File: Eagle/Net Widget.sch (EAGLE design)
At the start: 19 parts

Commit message: Switch to Net Widget.lbr and increase hole sizes.
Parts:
- U$2: device Weather Widget:ADAFRUIT-CC3000-BREAKOUT -> Net Widget:ADAFRUIT-CC3000-BREAKOUT
- U$3: device Weather Widget:ADAFRUIT-TFT1.8-BREAKOUT -> Net Widget:ADAFRUIT-TFT1.8-BREAKOUT
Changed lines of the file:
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@@
 <?xml version="1.0" encoding="utf-8"?>
 <!DOCTYPE eagle SYSTEM "eagle.dtd">
-<eagle version="7.1.0">
+<eagle version="7.2.0">
 <drawing>
 <settings>
@@
 <parts>
 <part name="U$1" library="adafruit" deviceset="ATMEGA32U4" device="-AU"/>
-<part name="U$2" library="Weather Widget" deviceset="ADAFRUIT-CC3000-BREAKOUT" device=""/>
-<part name="U$3" library="Weather Widget" deviceset="ADAFRUIT-TFT1.8-BREAKOUT" device=""/>
+<part name="U$2" library="Net Widget" deviceset="ADAFRUIT-CC3000-BREAKOUT" device=""/>
+<part name="U$3" library="Net Widget" deviceset="ADAFRUIT-TFT1.8-BREAKOUT" device=""/>
 <part name="ISP" library="adafruit" deviceset="AVRISP" device="-6"/>
 <part name="CN1" library="adafruit" deviceset="USB" device="MINIB"/>

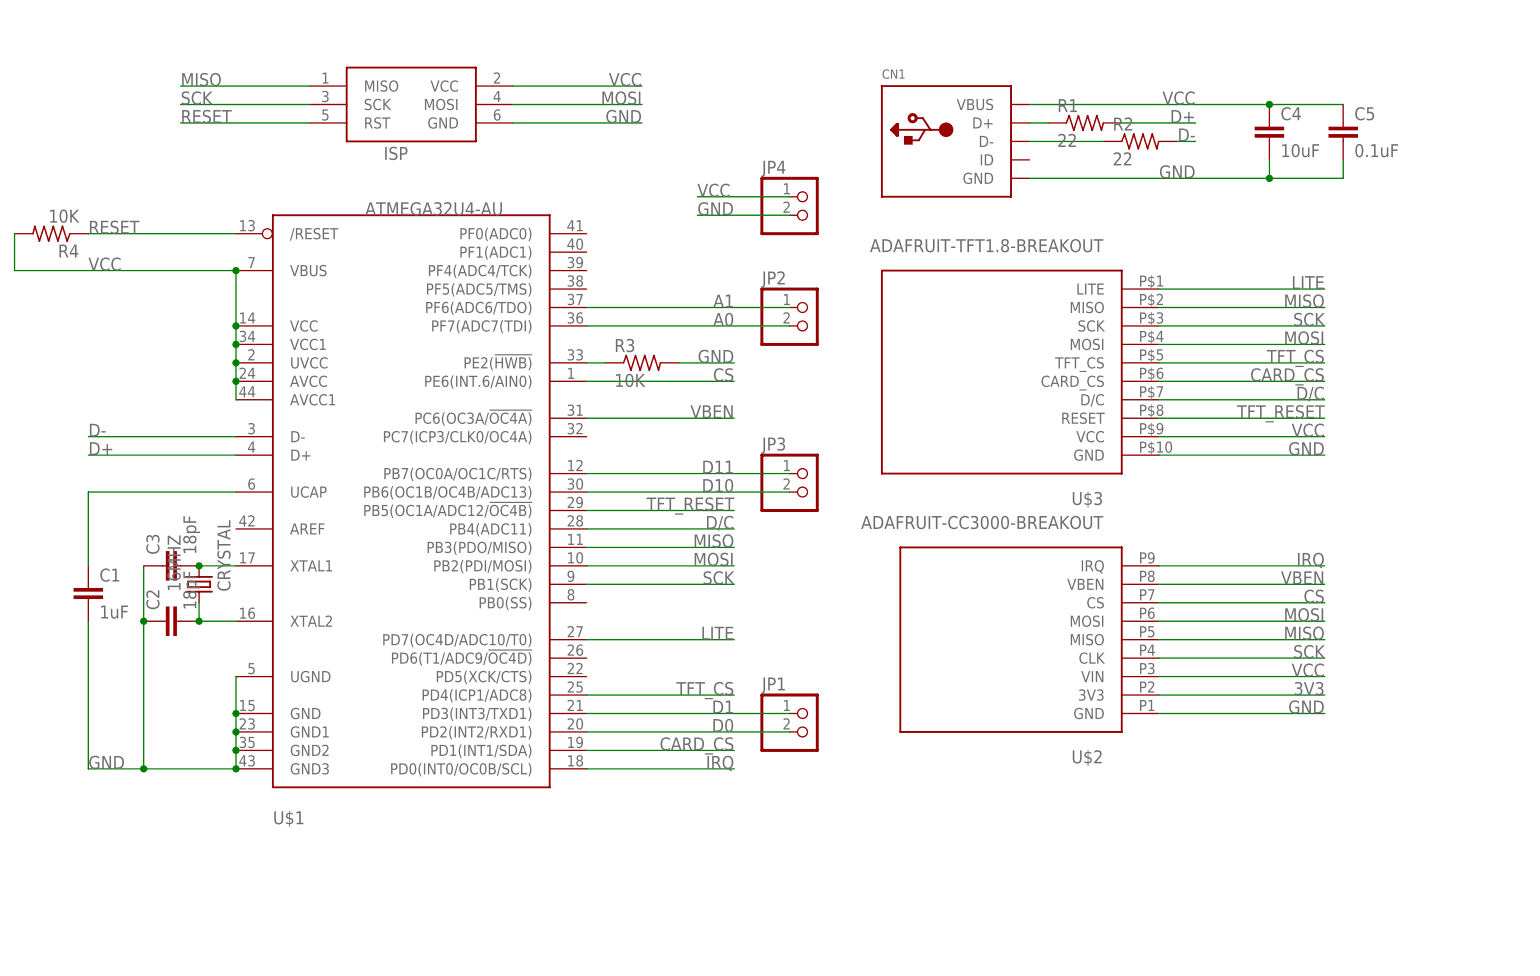
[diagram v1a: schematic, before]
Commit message: Replace ATmega32U4 w/ ATmega1284P.
Initial pass. Adds an FTDI header and replaces the Mini-USB footprint.
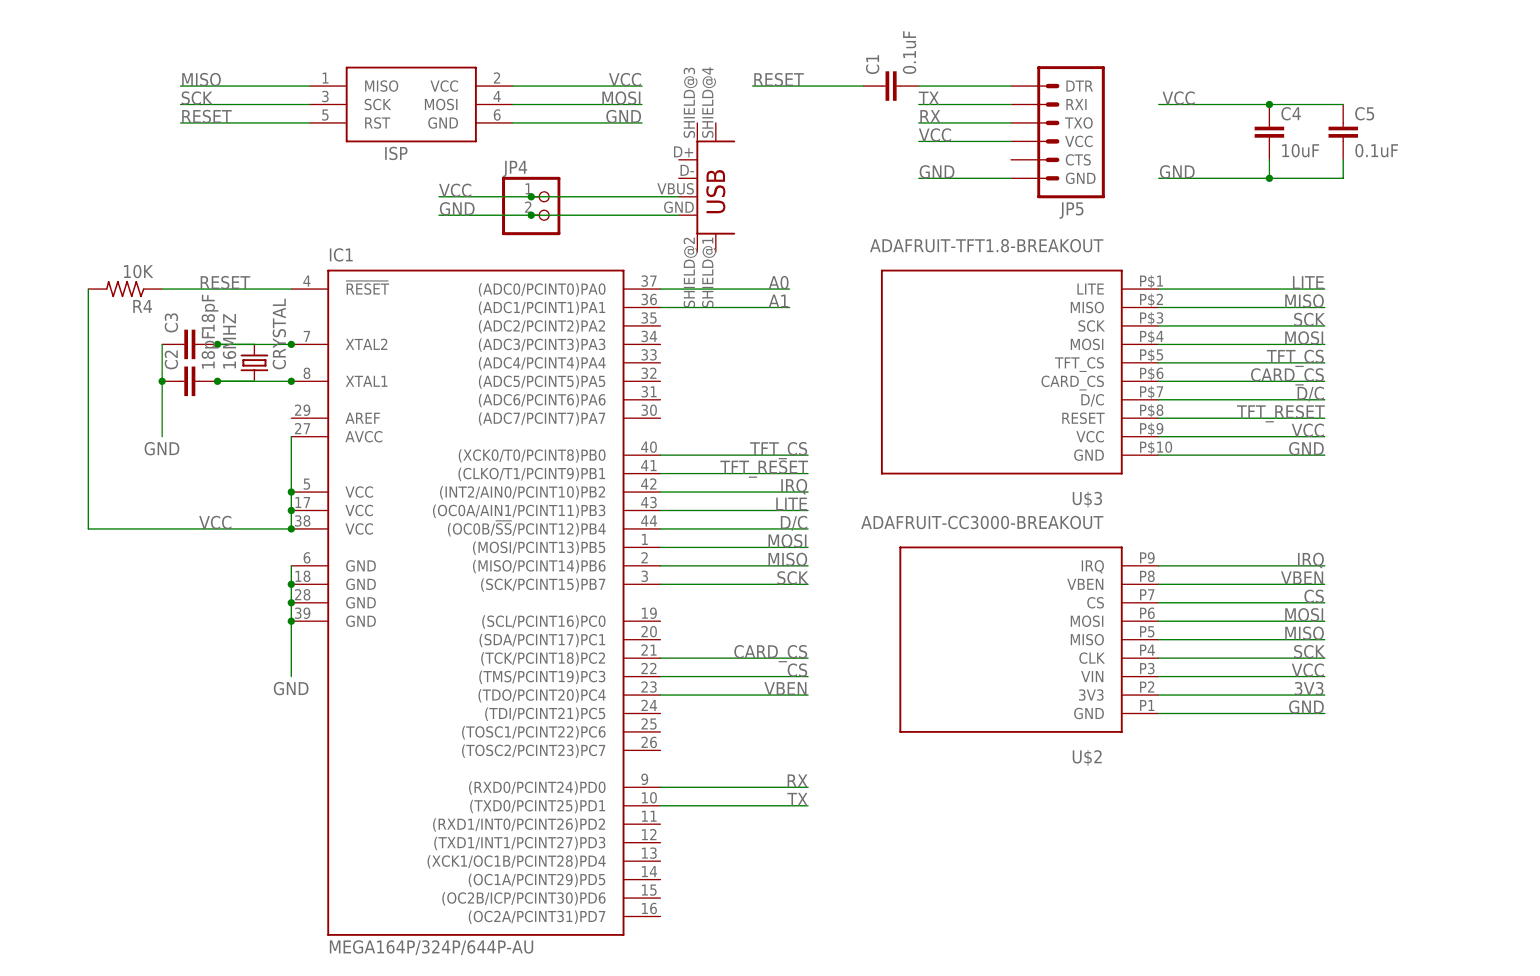
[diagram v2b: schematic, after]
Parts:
- removed CN1: (no value), adafruit:USBMINIB
- removed JP1, JP2, JP3: (no value), pinhead:PINHD-1X2
- removed R1, R2: 22, rcl:R-US_R1206
- removed R3: 10K, rcl:R-US_R1206
- added IC1: MEGA164P/324P/644P-AU, avr-5:MEGA164P/324P/644P-AU
- added JP5: (no value), SparkFun-Connectors:ARDUINO_SERIAL_PROGRAMPTH
- C1: value 1uF -> 0.1uF
- U$1: value ATMEGA32U4-AU -> USB_MINIB-POWER; device adafruit:ATMEGA32U4-AU -> Net Widget:USB_MINIB-POWER
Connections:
- removed net D+: R1.2, U$1.D+
- removed net D-: R2.2, U$1.D-
- removed net D0: JP1.2, U$1.PD2(INT2/RXD1)
- removed net D1: JP1.1, U$1.PD3(INT3/TXD1)
- removed net D10: JP3.2, U$1.PB6(OC1B/OC4B/ADC13)
- removed net D11: JP3.1, U$1.PB7(OC0A/OC1C/RTS)
- removed net N$2: CN1.D+, R1.1
- removed net N$3: CN1.D-, R2.1
- removed net N$4: C1.1, U$1.UCAP
- removed net N$5: R3.1, U$1.PE2(!HWB)
- new net N$1: C1.2, JP5.DTR
- new net RX: IC1.(RXD0/PCINT24)PD0, JP5.TXO
- new net TX: IC1.(TXD0/PCINT25)PD1, JP5.RXI
- net A0: now also IC1.(ADC0/PCINT0)PA0; no longer JP2.2, U$1.PF7(ADC7(TDI)
- net A1: now also IC1.(ADC1/PCINT1)PA1; no longer JP2.1, U$1.PF6(ADC6/TDO)
- net CARD_CS: now also IC1.(TCK/PCINT18)PC2; no longer U$1.PD1(INT1/SDA)
- net CS: now also IC1.(TMS/PCINT19)PC3; no longer U$1.PE6(INT.6/AIN0)
- net D/C: now also IC1.(OC0B/!SS!/PCINT12)PB4; no longer U$1.PB4(ADC11)
- net GND: now also IC1.GND@1, IC1.GND@2, IC1.GND@3, IC1.GND@4, JP5.GND; no longer C1.2, CN1.GND, R3.2, U$1.GND1, U$1.GND2, U$1.GND3, U$1.UGND
- net IRQ: now also IC1.(INT2/AIN0/PCINT10)PB2; no longer U$1.PD0(INT0/OC0B/SCL)
- net LITE: now also IC1.(OC0A/AIN1/PCINT11)PB3; no longer U$1.PD7(OC4D/ADC10/T0)
- net MISO: now also IC1.(MISO/PCINT14)PB6; no longer U$1.PB3(PDO/MISO)
- net MOSI: now also IC1.(MOSI/PCINT13)PB5; no longer U$1.PB2(PDI/MOSI)
- net N$6: now also IC1.XTAL2; no longer U$1.XTAL1
- net N$7: now also IC1.XTAL1; no longer U$1.XTAL2
- net RESET: now also C1.1, IC1.!RESET; no longer U$1./RESET
- net SCK: now also IC1.(SCK/PCINT15)PB7; no longer U$1.PB1(SCK)
- net TFT_CS: now also IC1.(XCK0/T0/PCINT8)PB0; no longer U$1.PD4(ICP1/ADC8)
- net TFT_RESET: now also IC1.(CLKO/T1/PCINT9)PB1; no longer U$1.PB5(OC1A/ADC12/!OC4B)
- net VBEN: now also IC1.(TDO/PCINT20)PC4; no longer U$1.PC6(OC3A/!OC4A)
- net VCC: now also IC1.AVCC, IC1.VCC@1, IC1.VCC@2, IC1.VCC@3, JP5.VCC; no longer CN1.VBUS, U$1.AVCC, U$1.AVCC1, U$1.UVCC, U$1.VCC, U$1.VCC1
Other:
- moved on the sheet: 16MHZ, C1, C2, C3, JP4, R4

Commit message: Clean up library and board.
Add breakout headers, move components into Net Widget library, switch
to Mini USB B connector with holes for mounting posts, silk screen
layout, etc.
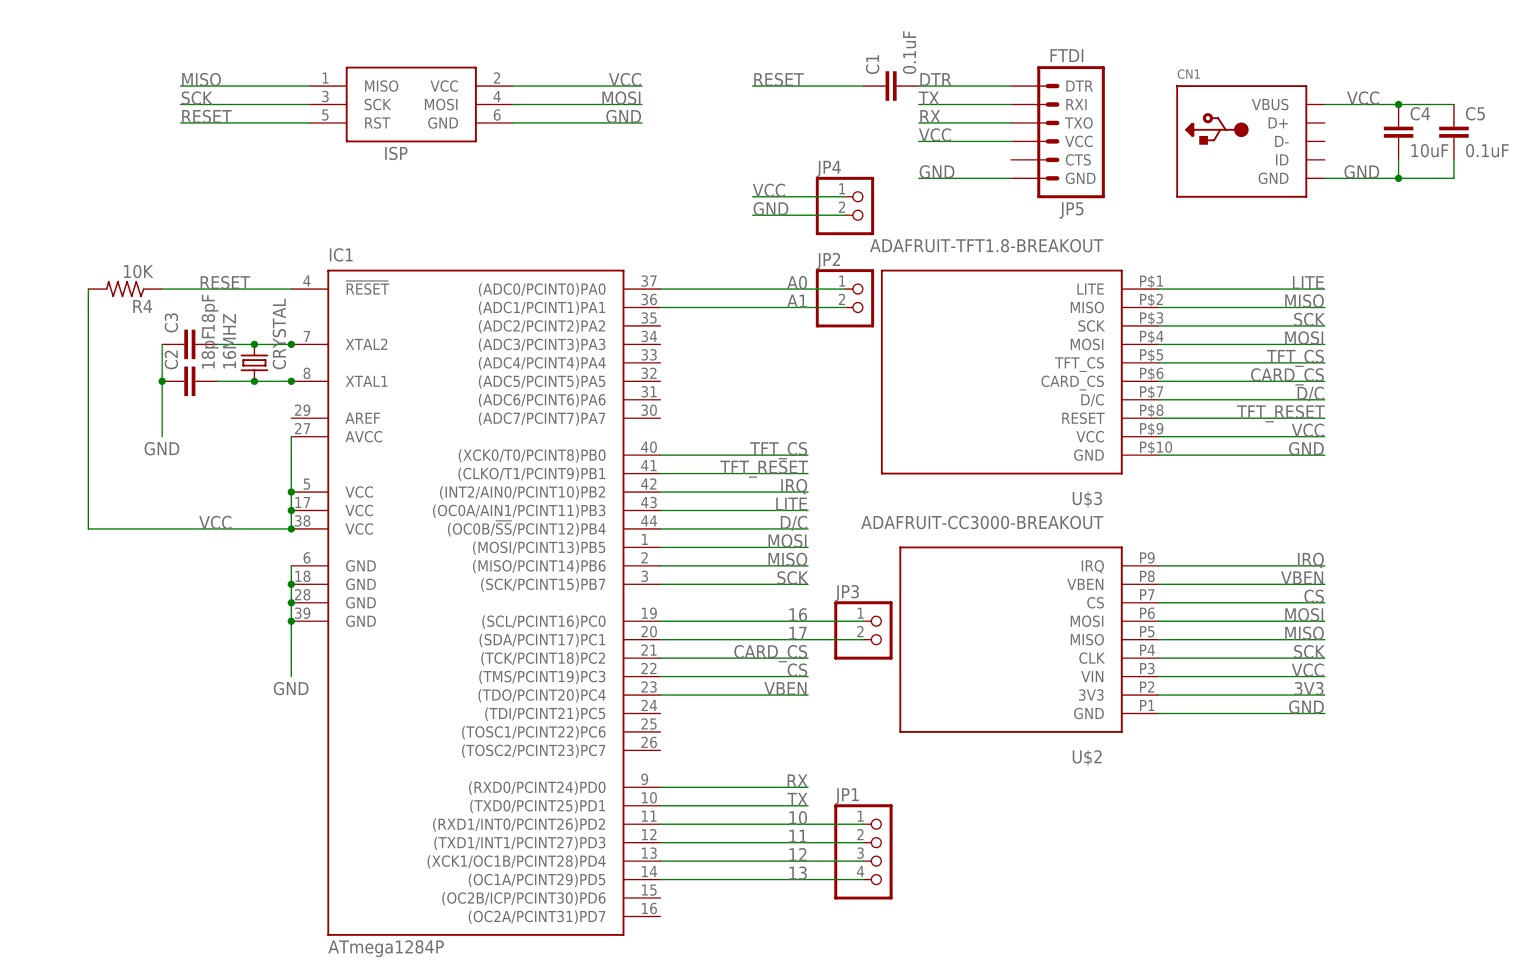
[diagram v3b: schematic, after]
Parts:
- removed U$1: USB_MINIB-POWER, Net Widget:USB_MINIB-POWER
- added CN1: (no value), Net Widget:USBPWR
- added JP1: (no value), pinhead:PINHD-1X4
- added JP2, JP3: (no value), pinhead:PINHD-1X2
- 16MHZ: device fab:CRYSTAL -> Net Widget:CRYSTAL
- IC1: value MEGA164P/324P/644P-AU -> ATmega1284P
- JP5: value (none) -> FTDI; device SparkFun-Connectors:ARDUINO_SERIAL_PROGRAMPTH -> Net Widget:ARDUINO_SERIAL_PROGRAMPTH
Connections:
- net N$1 renamed DTR
- new net 10: IC1.(RXD1/INT0/PCINT26)PD2, JP1.1
- new net 11: IC1.(TXD1/INT1/PCINT27)PD3, JP1.2
- new net 12: IC1.(XCK1/OC1B/PCINT28)PD4, JP1.3
- new net 13: IC1.(OC1A/PCINT29)PD5, JP1.4
- new net 16: IC1.(SCL/PCINT16)PC0, JP3.1
- new net 17: IC1.(SDA/PCINT17)PC1, JP3.2
- net A0: now also JP2.1
- net A1: now also JP2.2
- net GND: now also CN1.GND; no longer U$1.GND
- net VCC: now also CN1.VBUS; no longer U$1.VBUS
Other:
- moved on the sheet: C4, C5, JP4
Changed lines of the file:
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@@
 <part name="C4" library="rcl" deviceset="C-EU" device="C1206" value="10uF"/>
 <part name="C5" library="rcl" deviceset="C-EU" device="C1206" value="0.1uF"/>
-<part name="16MHZ" library="fab" deviceset="CRYSTAL" device=""/>
+<part name="16MHZ" library="Net Widget" deviceset="CRYSTAL" device=""/>
 <part name="JP4" library="pinhead" deviceset="PINHD-1X2" device=""/>
 <part name="R4" library="rcl" deviceset="R-US_" device="R1206" value="10K"/>
-<part name="IC1" library="avr-5" deviceset="MEGA164P/324P/644P-AU" device=""/>
-<part name="JP5" library="SparkFun-Connectors" deviceset="ARDUINO_SERIAL_PROGRAM" device="PTH"/>
+<part name="IC1" library="avr-5" deviceset="MEGA164P/324P/644P-AU" device="" value="ATmega1284P"/>
+<part name="JP5" library="Net Widget" deviceset="ARDUINO_SERIAL_PROGRAM" device="PTH" value="FTDI"/>
 <part name="C1" library="rcl" deviceset="C-EU" device="C1206" value="0.1uF"/>
-<part name="U$1" library="Net Widget" deviceset="USB_MINIB" device="-POWER"/>
+<part name="JP1" library="pinhead" deviceset="PINHD-1X4" device=""/>
+<part name="JP2" library="pinhead" deviceset="PINHD-1X2" device=""/>
+<part name="JP3" library="pinhead" deviceset="PINHD-1X2" device=""/>
+<part name="CN1" library="Net Widget" deviceset="USB" device="PWR"/>
 </parts>
 <sheets>
@@
 <instance part="C2" gate="G$1" x="17.78" y="68.58" rot="R90"/>
 <instance part="C3" gate="G$1" x="17.78" y="73.66" rot="R90"/>
-<instance part="C4" gate="G$1" x="167.64" y="104.14"/>
-<instance part="C5" gate="G$1" x="177.8" y="104.14"/>
+<instance part="C4" gate="G$1" x="185.42" y="104.14"/>
+<instance part="C5" gate="G$1" x="193.04" y="104.14"/>
 <instance part="16MHZ" gate="G$1" x="27.94" y="71.12" rot="R90"/>
-<instance part="JP4" gate="G$1" x="68.58" y="91.44"/>
+<instance part="JP4" gate="G$1" x="111.76" y="91.44"/>
 <instance part="R4" gate="G$1" x="10.16" y="81.28" rot="R180"/>
 <instance part="IC1" gate="G$1" x="58.42" y="38.1"/>
 <instance part="JP5" gate="G$1" x="137.16" y="104.14" rot="R180"/>
 <instance part="C1" gate="G$1" x="114.3" y="109.22" rot="R90"/>
-<instance part="U$1" gate="G$1" x="88.9" y="96.52"/>
+<instance part="JP1" gate="A" x="114.3" y="2.54"/>
+<instance part="JP2" gate="G$1" x="111.76" y="78.74"/>
+<instance part="JP3" gate="G$1" x="114.3" y="33.02"/>
+<instance part="CN1" gate="G$1" x="165.1" y="101.6"/>
 </instances>
 <busses>
@@
 </segment>
 <segment>
-<wire x1="152.4" y1="96.52" x2="167.64" y2="96.52" width="0.1524" layer="91"/>
-<label x="157.48" y="96.52" size="1.778" layer="95" rot="MR0"/>
+<wire x1="175.26" y1="96.52" x2="185.42" y2="96.52" width="0.1524" layer="91"/>
+<label x="182.88" y="96.52" size="1.778" layer="95" rot="MR0"/>
 <pinref part="C4" gate="G$1" pin="2"/>
-<wire x1="167.64" y1="96.52" x2="167.64" y2="99.06" width="0.1524" layer="91"/>
+<wire x1="185.42" y1="96.52" x2="185.42" y2="99.06" width="0.1524" layer="91"/>
 <pinref part="C5" gate="G$1" pin="2"/>
-<wire x1="167.64" y1="96.52" x2="177.8" y2="96.52" width="0.1524" layer="91"/>
-<wire x1="177.8" y1="96.52" x2="177.8" y2="99.06" width="0.1524" layer="91"/>
-<junction x="167.64" y="96.52"/>
+<wire x1="185.42" y1="96.52" x2="193.04" y2="96.52" width="0.1524" layer="91"/>
+<wire x1="193.04" y1="96.52" x2="193.04" y2="99.06" width="0.1524" layer="91"/>
+<junction x="185.42" y="96.52"/>
+<pinref part="CN1" gate="G$1" pin="GND"/>
 </segment>
 <segment>
 <pinref part="JP4" gate="G$1" pin="2"/>
-<wire x1="66.04" y1="91.44" x2="53.34" y2="91.44" width="0.1524" layer="91"/>
-<label x="53.34" y="91.44" size="1.778" layer="95"/>
-<pinref part="U$1" gate="G$1" pin="GND"/>
-<wire x1="66.04" y1="91.44" x2="86.36" y2="91.44" width="0.1524" layer="91"/>
-<junction x="66.04" y="91.44"/>
+<wire x1="109.22" y1="91.44" x2="96.52" y2="91.44" width="0.1524" layer="91"/>
+<label x="96.52" y="91.44" size="1.778" layer="95"/>
 </segment>
 <segment>
@@
 </segment>
 <segment>
-<wire x1="152.4" y1="106.68" x2="167.64" y2="106.68" width="0.1524" layer="91"/>
-<label x="157.48" y="106.68" size="1.778" layer="95" rot="MR0"/>
+<wire x1="175.26" y1="106.68" x2="185.42" y2="106.68" width="0.1524" layer="91"/>
+<label x="182.88" y="106.68" size="1.778" layer="95" rot="MR0"/>
 <pinref part="C4" gate="G$1" pin="1"/>
 <pinref part="C5" gate="G$1" pin="1"/>
-<wire x1="167.64" y1="106.68" x2="177.8" y2="106.68" width="0.1524" layer="91"/>
-<junction x="167.64" y="106.68"/>
+<wire x1="185.42" y1="106.68" x2="193.04" y2="106.68" width="0.1524" layer="91"/>
+<junction x="185.42" y="106.68"/>
+<pinref part="CN1" gate="G$1" pin="VBUS"/>
 </segment>
 <segment>
@@
 <segment>
 <pinref part="JP4" gate="G$1" pin="1"/>
-<wire x1="66.04" y1="93.98" x2="53.34" y2="93.98" width="0.1524" layer="91"/>
-<label x="53.34" y="93.98" size="1.778" layer="95"/>
-<pinref part="U$1" gate="G$1" pin="VBUS"/>
-<wire x1="66.04" y1="93.98" x2="86.36" y2="93.98" width="0.1524" layer="91"/>
-<junction x="66.04" y="93.98"/>
+<wire x1="109.22" y1="93.98" x2="96.52" y2="93.98" width="0.1524" layer="91"/>
+<label x="96.52" y="93.98" size="1.778" layer="95"/>
 </segment>
 <segment>
@@
 <junction x="33.02" y="73.66"/>
 <pinref part="IC1" gate="G$1" pin="XTAL2"/>
-<wire x1="33.02" y1="73.66" x2="22.86" y2="73.66" width="0.1524" layer="91"/>
-<junction x="22.86" y="73.66"/>
-<wire x1="22.86" y1="73.66" x2="27.94" y2="73.66" width="0.1524" layer="91"/>
+<wire x1="33.02" y1="73.66" x2="27.94" y2="73.66" width="0.1524" layer="91"/>
+<junction x="27.94" y="73.66"/>
+<wire x1="27.94" y1="73.66" x2="22.86" y2="73.66" width="0.1524" layer="91"/>
 </segment>
 </net>
@@
 <junction x="33.02" y="68.58"/>
 <pinref part="IC1" gate="G$1" pin="XTAL1"/>
-<wire x1="33.02" y1="68.58" x2="22.86" y2="68.58" width="0.1524" layer="91"/>
-<junction x="22.86" y="68.58"/>
-<wire x1="22.86" y1="68.58" x2="27.94" y2="68.58" width="0.1524" layer="91"/>
+<wire x1="33.02" y1="68.58" x2="27.94" y2="68.58" width="0.1524" layer="91"/>
+<junction x="27.94" y="68.58"/>
+<wire x1="27.94" y1="68.58" x2="22.86" y2="68.58" width="0.1524" layer="91"/>
 </segment>
 </net>
@@
 <segment>
 <pinref part="IC1" gate="G$1" pin="(ADC1/PCINT1)PA1"/>
-<wire x1="83.82" y1="78.74" x2="101.6" y2="78.74" width="0.1524" layer="91"/>
-<label x="101.6" y="78.74" size="1.778" layer="95" rot="MR0"/>
+<wire x1="83.82" y1="78.74" x2="109.22" y2="78.74" width="0.1524" layer="91"/>
+<label x="104.14" y="78.74" size="1.778" layer="95" rot="MR0"/>
+<pinref part="JP2" gate="G$1" pin="2"/>
 </segment>
 </net>
@@
 <segment>
 <pinref part="IC1" gate="G$1" pin="(ADC0/PCINT0)PA0"/>
-<wire x1="83.82" y1="81.28" x2="101.6" y2="81.28" width="0.1524" layer="91"/>
-<label x="101.6" y="81.28" size="1.778" layer="95" rot="MR0"/>
-</segment>
-</net>
-<net name="N$1" class="0">
+<wire x1="83.82" y1="81.28" x2="109.22" y2="81.28" width="0.1524" layer="91"/>
+<label x="104.14" y="81.28" size="1.778" layer="95" rot="MR0"/>
+<pinref part="JP2" gate="G$1" pin="1"/>
+</segment>
+</net>
+<net name="DTR" class="0">
 <segment>
 <pinref part="JP5" gate="G$1" pin="DTR"/>
 <pinref part="C1" gate="G$1" pin="2"/>
 <wire x1="119.38" y1="109.22" x2="132.08" y2="109.22" width="0.1524" layer="91"/>
+<label x="119.38" y="109.22" size="1.778" layer="95"/>
 </segment>
 </net>
@@
 </segment>
 </net>
+<net name="10" class="0">
+<segment>
+<pinref part="IC1" gate="G$1" pin="(RXD1/INT0/PCINT26)PD2"/>
+<pinref part="JP1" gate="A" pin="1"/>
+<wire x1="111.76" y1="7.62" x2="83.82" y2="7.62" width="0.1524" layer="91"/>
+<label x="104.14" y="7.62" size="1.778" layer="95" rot="MR0"/>
+</segment>
+</net>
+<net name="11" class="0">
+<segment>
+<pinref part="IC1" gate="G$1" pin="(TXD1/INT1/PCINT27)PD3"/>
+<pinref part="JP1" gate="A" pin="2"/>
+<wire x1="111.76" y1="5.08" x2="83.82" y2="5.08" width="0.1524" layer="91"/>
+<label x="104.14" y="5.08" size="1.778" layer="95" rot="MR0"/>
+</segment>
+</net>
+<net name="12" class="0">
+<segment>
+<pinref part="IC1" gate="G$1" pin="(XCK1/OC1B/PCINT28)PD4"/>
+<pinref part="JP1" gate="A" pin="3"/>
+<wire x1="111.76" y1="2.54" x2="83.82" y2="2.54" width="0.1524" layer="91"/>
+<label x="104.14" y="2.54" size="1.778" layer="95" rot="MR0"/>
+</segment>
+</net>
+<net name="13" class="0">
+<segment>
+<pinref part="IC1" gate="G$1" pin="(OC1A/PCINT29)PD5"/>
+<pinref part="JP1" gate="A" pin="4"/>
+<wire x1="111.76" y1="0" x2="83.82" y2="0" width="0.1524" layer="91"/>
+<label x="104.14" y="0" size="1.778" layer="95" rot="MR0"/>
+</segment>
+</net>
+<net name="16" class="0">
+<segment>
+<pinref part="IC1" gate="G$1" pin="(SCL/PCINT16)PC0"/>
+<pinref part="JP3" gate="G$1" pin="1"/>
+<wire x1="111.76" y1="35.56" x2="83.82" y2="35.56" width="0.1524" layer="91"/>
+<label x="104.14" y="35.56" size="1.778" layer="95" rot="MR0"/>
+</segment>
+</net>
+<net name="17" class="0">
+<segment>
+<pinref part="IC1" gate="G$1" pin="(SDA/PCINT17)PC1"/>
+<pinref part="JP3" gate="G$1" pin="2"/>
+<wire x1="111.76" y1="33.02" x2="83.82" y2="33.02" width="0.1524" layer="91"/>
+<label x="104.14" y="33.02" size="1.778" layer="95" rot="MR0"/>
+</segment>
+</net>
